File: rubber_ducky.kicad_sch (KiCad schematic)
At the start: 1 part, among them U1 MK20DX128VFM5

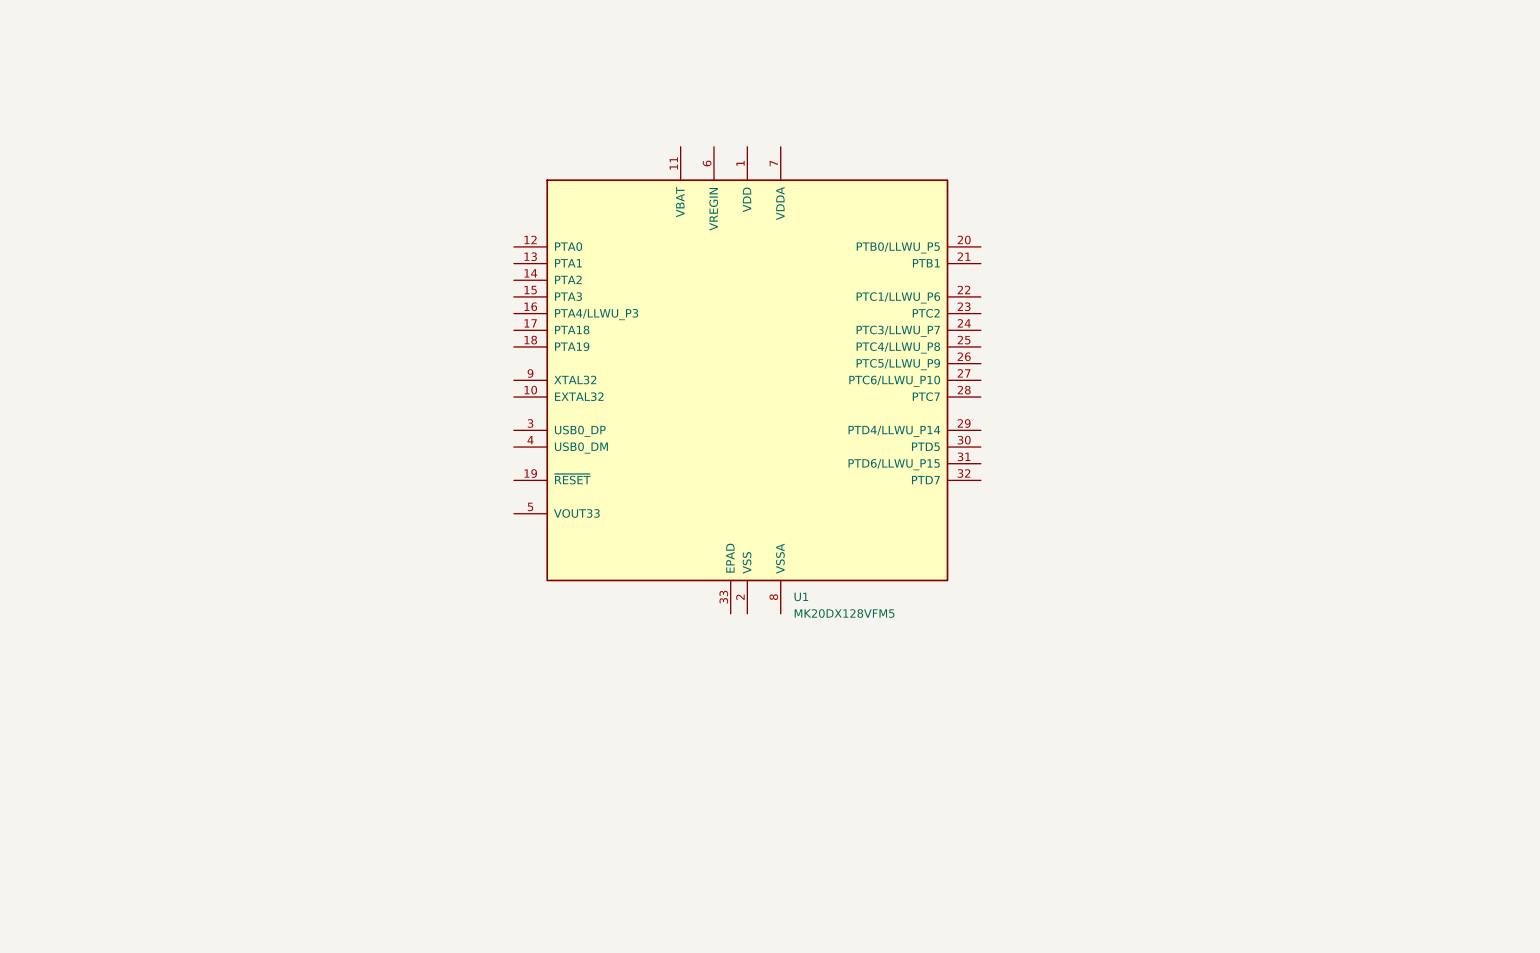
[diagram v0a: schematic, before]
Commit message: adding component in schmatics
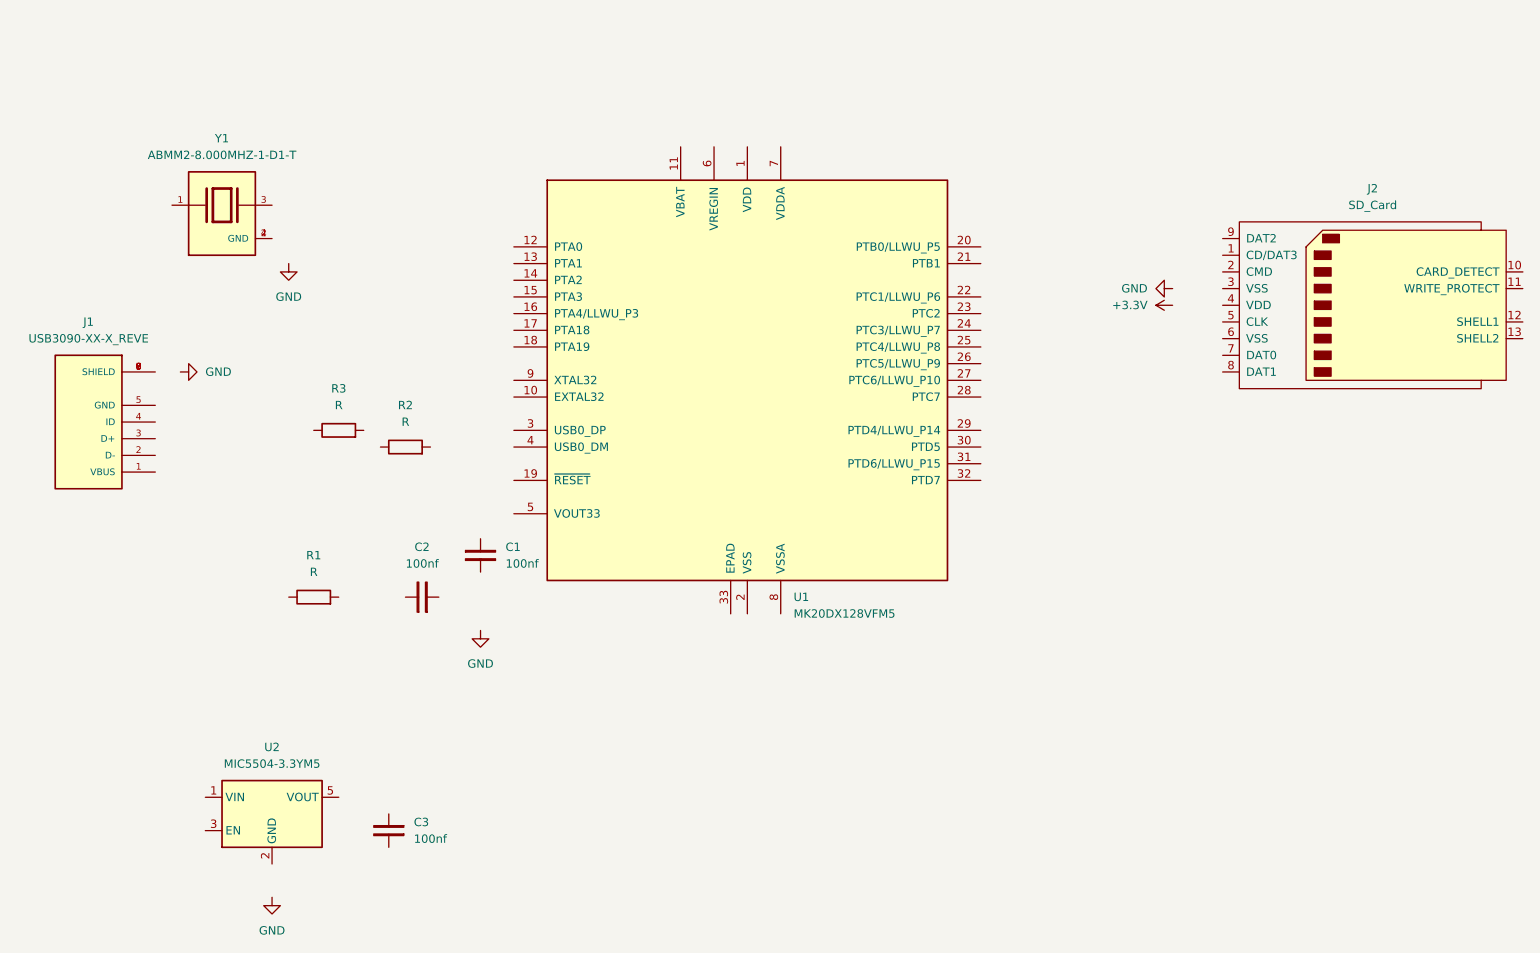
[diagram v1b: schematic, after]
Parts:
- added C1, C2, C3: 100nf, Capacitor_THT:C_Disc_D3.0mm_W2.0mm_P2.50mm, symbol PCM_SL_Devices:Capacitor_NP
- added J1: USB3090-XX-X_REVE, USB3090-XX-X_REVE:GCT_USB3090-XX-X_REVE, symbol USB3090-XX-X_REVE:USB3090-XX-X_REVE
- added J2: SD_Card, symbol Connector:SD_Card
- added R1, R2, R3: R, symbol Device:R
- added U2: MIC5504-3.3YM5, Package_TO_SOT_SMD:SOT-23-5, symbol Regulator_Linear:MIC5504-3.3YM5
- added Y1: ABMM2-8.000MHZ-1-D1-T, ABMM2-8.000MHZ-1-D1-T:XTAL_ABMM2-8.000MHZ-1-D1-T, symbol ABMM2-8.000MHZ-1-D1-T:ABMM2-8.000MHZ-1-D1-T
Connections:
- new net: Y1.2 (GND), Y1.4 (GND)
- new net: J1.6 (SHIELD), J1.7 (SHIELD), J1.8 (SHIELD), J1.9 (SHIELD)

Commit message: workied_on_connection
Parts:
- added C4: Capacitor_NP, Capacitor_THT:C_Disc_D3.0mm_W2.0mm_P2.50mm, symbol PCM_SL_Devices:Capacitor_NP
- R3: value R -> 30R
- renumbered R2 to 30R
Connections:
- net +3.3V: now also J2.4 (VDD)
- net GND: now also C1.1, C2.1, C3.2, J1.5 (GND), J1.6 (SHIELD), J1.7 (SHIELD), J1.8 (SHIELD), J1.9 (SHIELD), J2.3 (VSS), J2.6 (VSS), U1.2 (VSS), U1.33 (EPAD), U1.8 (VSSA), U2.2 (GND), Y1.2 (GND), Y1.4 (GND), C4.1
- net CS: now reaches J2.1 (CD/DAT3)
- net CS: now also U1.25 (PTC4/LLWU_P8)
- net MOSI: now reaches J2.2 (CMD)
- net MOSI: now also U1.27 (PTC6/LLWU_P10)
- net SCLK: now reaches J2.5 (CLK)
- net SCLK: now also U1.26 (PTC5/LLWU_P9)
- net MISO: now reaches J2.7 (DAT0)
- net MISO: now also U1.28 (PTC7)
- net USB_DW: now reaches 30R.1
- net USB_DW: now also J1.2 (D-)
- net at 30R.2: now also U1.4 (USB0_DM)
- net at C2.2: now also R1.2
- net +3V3: now reaches U1.1 (VDD)
- net +3V3: now also C3.1, R1.1, U1.7 (VDDA), U2.5 (VOUT), C4.2
- net PTA18: now reaches U1.17 (PTA18)
- net PTA18: now also Y1.3
- net PTA19: now reaches U1.18 (PTA19)
- net PTA19: now also Y1.1
- net at U1.3 (USB0_DP): now also R3.2
- net RST: now reaches U1.5 (VOUT33)
- net RST: now also C1.2
- net VBUS: now reaches U1.6 (VREGIN)
- net VBUS: now also J1.1 (VBUS), U2.1 (VIN), U2.3 (EN)
- net USB_DP: now reaches J1.3 (D+)
- net USB_DP: now also R3.1
- no-connect marks 0 -> 25
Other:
- moved on the sheet: 30R, R3
